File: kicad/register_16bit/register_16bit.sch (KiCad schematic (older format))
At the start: 0 parts

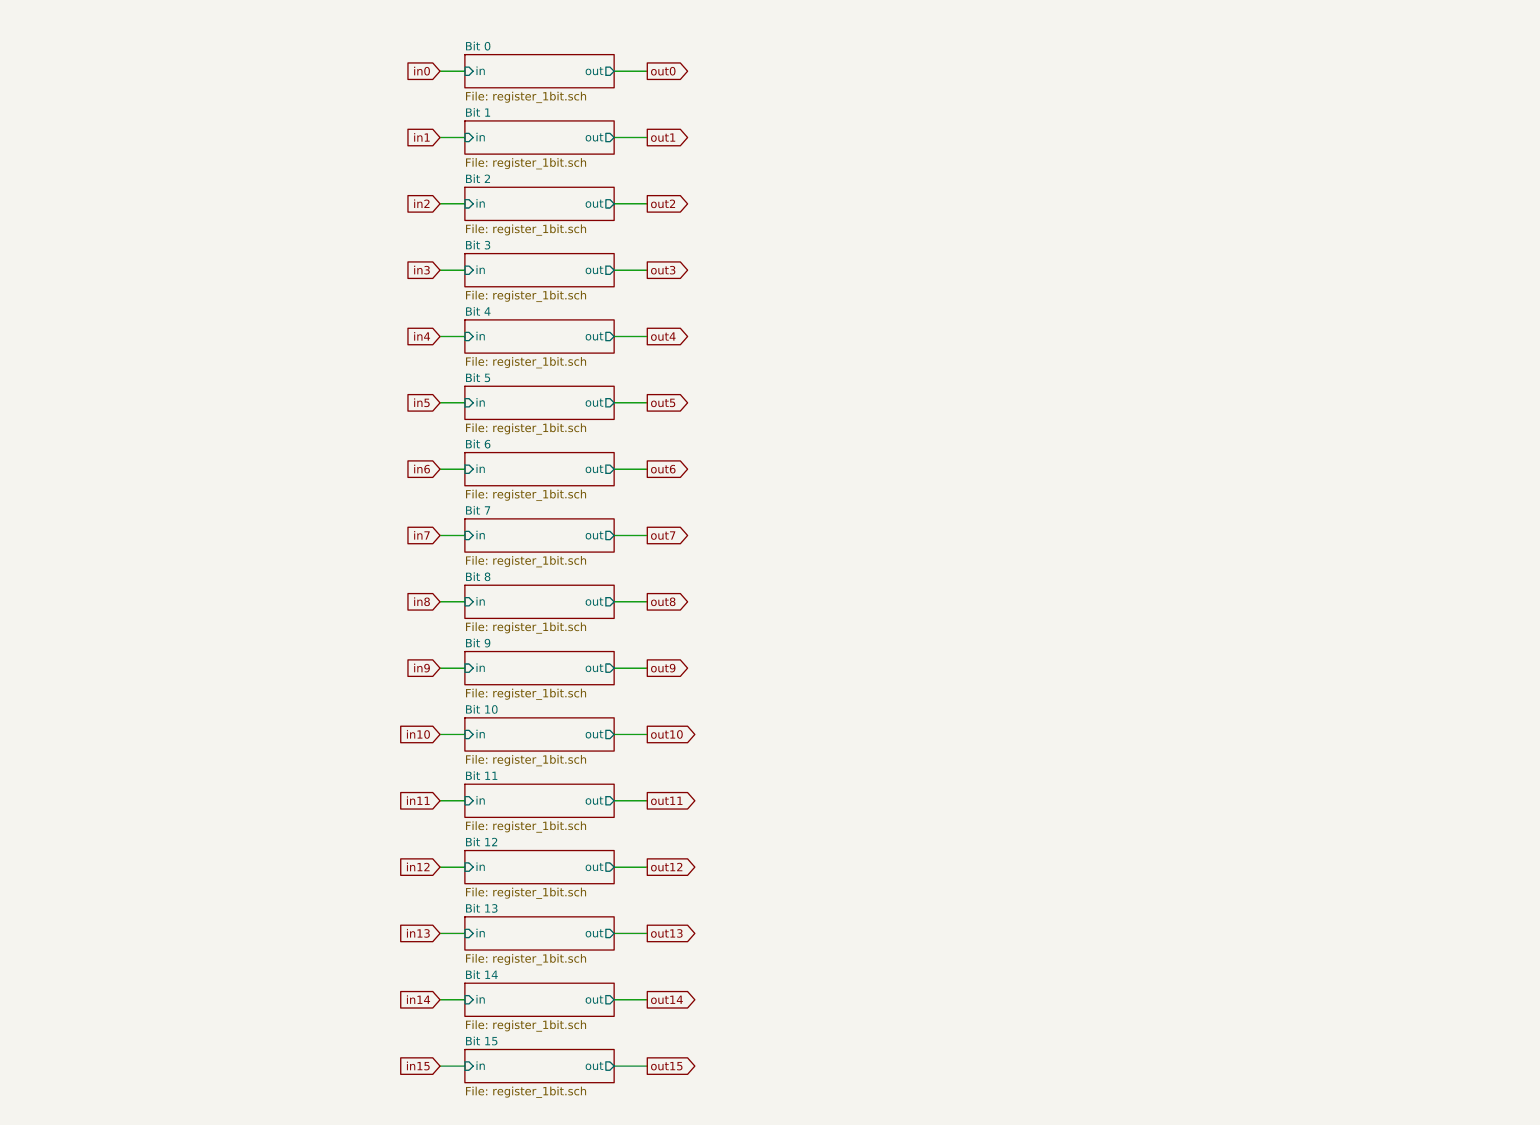
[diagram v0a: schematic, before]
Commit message: Finished initial PCB layout and routing for 16-bit register.
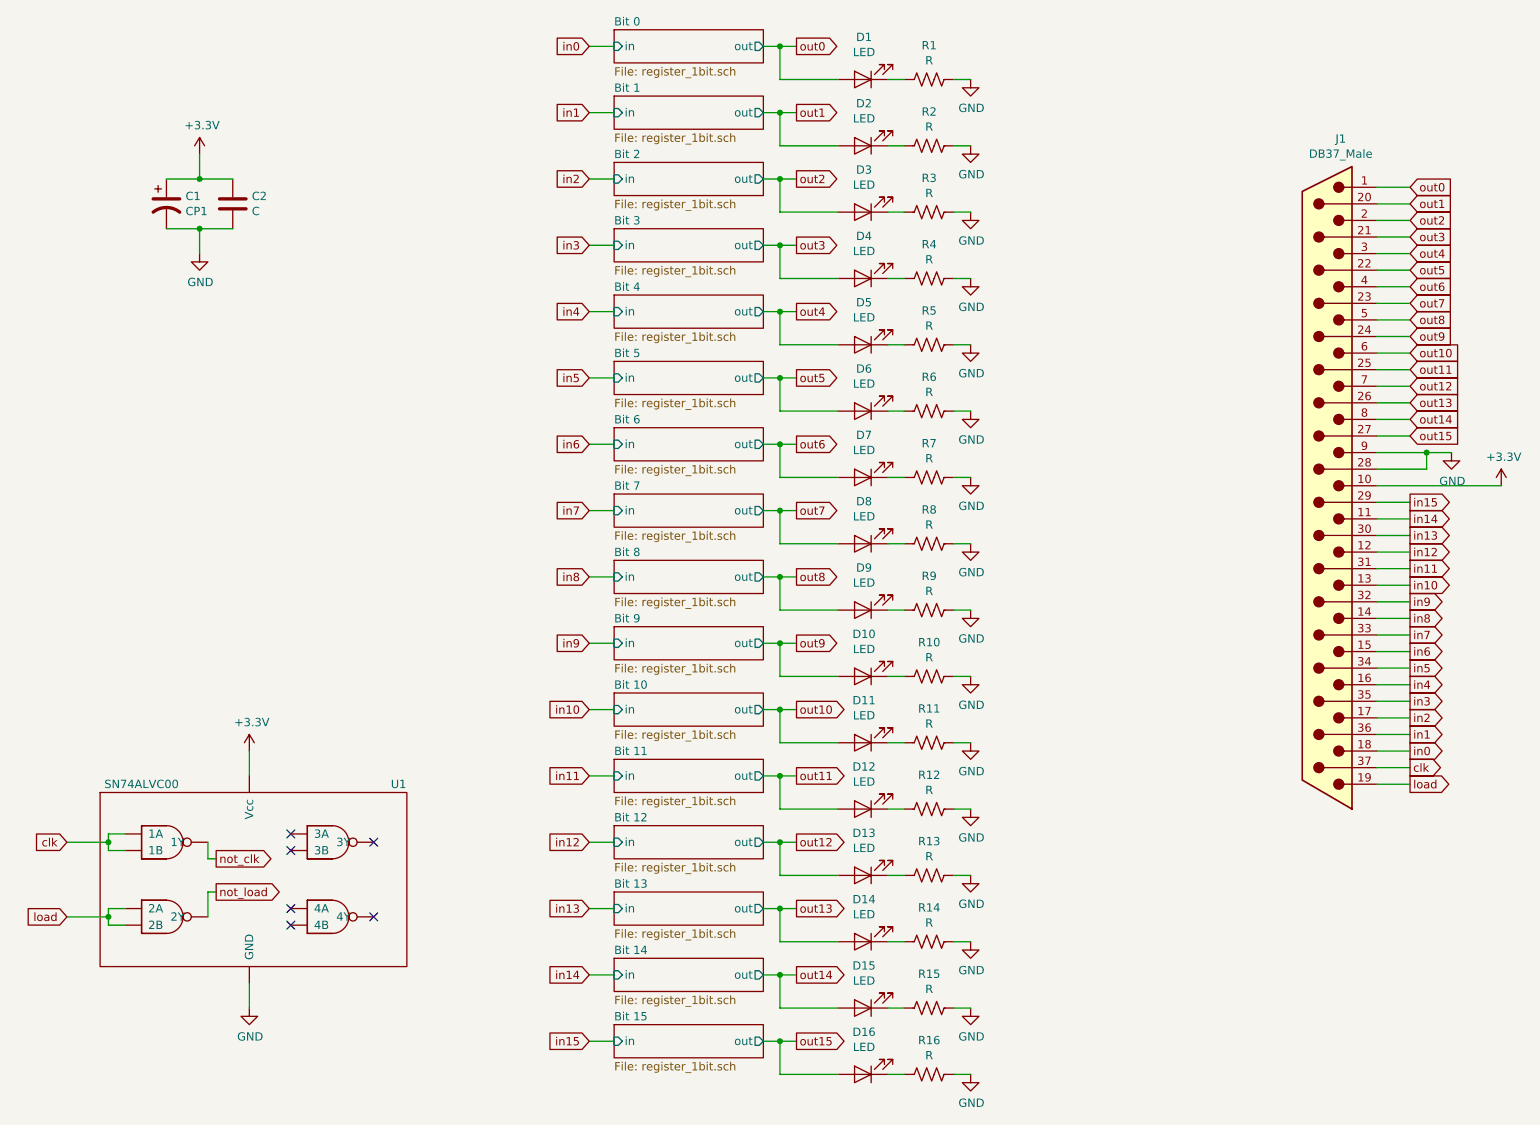
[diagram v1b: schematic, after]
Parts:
- added C1: CP1, Capacitor_THT:CP_Radial_D8.0mm_P2.50mm, symbol Device:CP1
- added C2: C, Capacitor_THT:C_Disc_D5.0mm_W2.5mm_P2.50mm, symbol Device:C
- added D1, D10, D11, D12, D13, D14, D15, D16, D2, D3, D4, D5, D6, D7, D8, D9: LED, LED_THT:LED_D5.0mm, symbol Device:LED
- added J1: DB37_Male, Connector_Dsub:DSUB-37_Male_Horizontal_P2.77x2.84mm_EdgePinOffset4.94mm_Housed_MountingHolesOffset7.48mm, symbol Connector:DB37_Male
- added R1, R10, R11, R12, R13, R14, R15, R16, R2, R3, R4, R5, R6, R7, R8, R9: R, Resistor_SMD:R_1206_3216Metric, symbol Device:R_US
- added U1: SN74ALVC00, Package_SO:TSSOP-14_4.4x5mm_P0.65mm, symbol NANDIRL_components:SN74ALVC00
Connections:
- net in0: now also J1.18
- net in1: now also J1.36
- net in10: now also J1.13
- net in11: now also J1.31
- net in12: now also J1.12
- net in13: now also J1.30
- net in14: now also J1.11
- net in15: now also J1.29
- net in2: now also J1.17
- net in3: now also J1.35
- net in4: now also J1.16
- net in5: now also J1.34
- net in6: now also J1.15
- net in7: now also J1.33
- net in8: now also J1.14
- net in9: now also J1.32
- net out0: now also D1.2 (A), J1.1
- net out1: now also D2.2 (A), J1.20
- net out10: now also D11.2 (A), J1.6
- net out11: now also D12.2 (A), J1.25
- net out12: now also D13.2 (A), J1.7
- net out13: now also D14.2 (A), J1.26
- net out14: now also D15.2 (A), J1.8
- net out15: now also D16.2 (A), J1.27
- net out2: now also D3.2 (A), J1.2
- net out3: now also D4.2 (A), J1.21
- net out4: now also D5.2 (A), J1.3
- net out5: now also D6.2 (A), J1.22
- net out6: now also D7.2 (A), J1.4
- net out7: now also D8.2 (A), J1.23
- net out8: now also D9.2 (A), J1.5
- net out9: now also D10.2 (A), J1.24
- new net: D1.1 (K), R1.2
- new net: D2.1 (K), R2.2
- new net: D3.1 (K), R3.2
- new net: D4.1 (K), R4.2
- new net: D5.1 (K), R5.2
- new net: D6.1 (K), R6.2
- new net: D7.1 (K), R7.2
- new net: D8.1 (K), R8.2
- new net: D9.1 (K), R9.2
- new net: D10.1 (K), R10.2
- new net: D11.1 (K), R11.2
- new net: D12.1 (K), R12.2
- new net: D13.1 (K), R13.2
- new net: D14.1 (K), R14.2
- new net: D15.1 (K), R15.2
- new net: D16.1 (K), R16.2
- new net +3V3: C1.1, C2.1, J1.10, U1.14 (Vcc)
- new net GND: C1.2, C2.2, J1.28, J1.9, R1.1, R10.1, R11.1, R12.1, R13.1, R14.1, R15.1, R16.1, R2.1, R3.1, R4.1, R5.1, R6.1, R7.1, R8.1, R9.1, U1.7 (GND)
- new net clk: J1.37, U1.1 (1A), U1.2 (1B)
- new net load: J1.19, U1.4 (2A), U1.5 (2B)
- new net not_clk: U1.3 (1Y)
- new net not_load: U1.6 (2Y)
- no-connect marks 0 -> 6

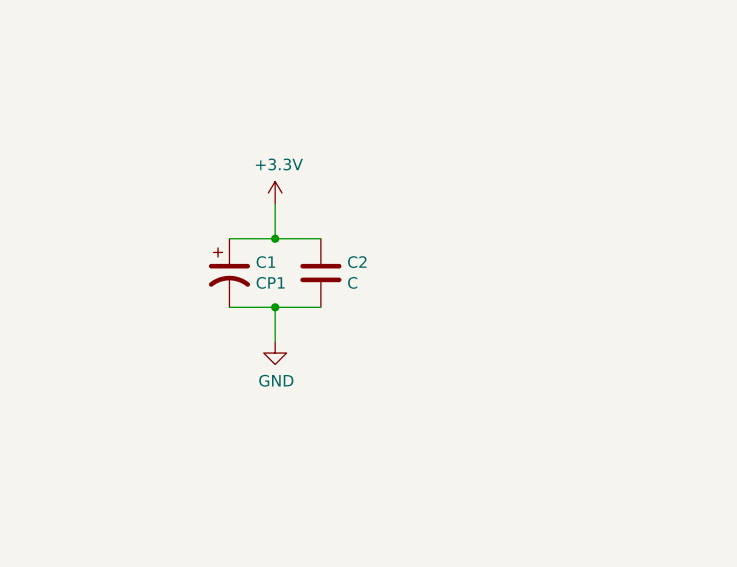
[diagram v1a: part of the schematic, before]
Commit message: Added clock generator, tested on breadboard. Added motherboard, routing unfinished. Various component updates.
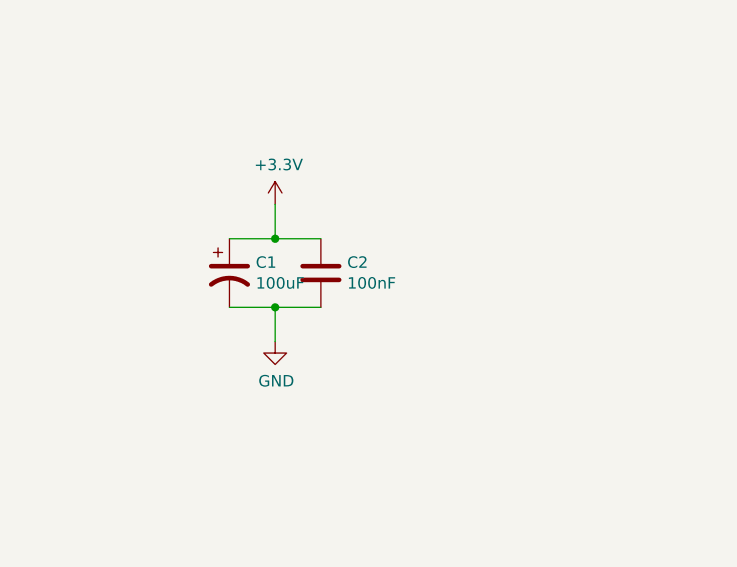
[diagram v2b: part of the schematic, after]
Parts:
- C1: value CP1 -> 100uF; Digikey PN (none) -> P15797CT-ND
- C2: value C -> 100nF; footprint Capacitor_THT:C_Disc_D5.0mm_W2.5mm_P2.50mm -> Capacitor_THT:C_Disc_D5.0mm_W2.5mm_P5.00mm; Digikey PN (none) -> BC5229CT-ND
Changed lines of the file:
@@
 P 1650 2000
 F 0 "C1" H 1765 2046 50  0000 L CNN
-F 1 "CP1" H 1765 1955 50  0000 L CNN
+F 1 "100uF" H 1765 1955 50  0000 L CNN
 F 2 "Capacitor_THT:CP_Radial_D8.0mm_P2.50mm" H 1650 2000 50  0001 C CNN
 F 3 "~" H 1650 2000 50  0001 C CNN
+F 4 "P15797CT-ND" H 1650 2000 50  0001 C CNN "Digikey PN"
 	1    1650 2000
 	1    0    0    -1
@@
 P 2050 2000
 F 0 "C2" H 2165 2046 50  0000 L CNN
-F 1 "C" H 2165 1955 50  0000 L CNN
-F 2 "Capacitor_THT:C_Disc_D5.0mm_W2.5mm_P2.50mm" H 2088 1850 50  0001 C CNN
+F 1 "100nF" H 2165 1955 50  0000 L CNN
+F 2 "Capacitor_THT:C_Disc_D5.0mm_W2.5mm_P5.00mm" H 2088 1850 50  0001 C CNN
 F 3 "~" H 2050 2000 50  0001 C CNN
+F 4 "BC5229CT-ND" H 2050 2000 50  0001 C CNN "Digikey PN"
 	1    2050 2000
 	1    0    0    -1

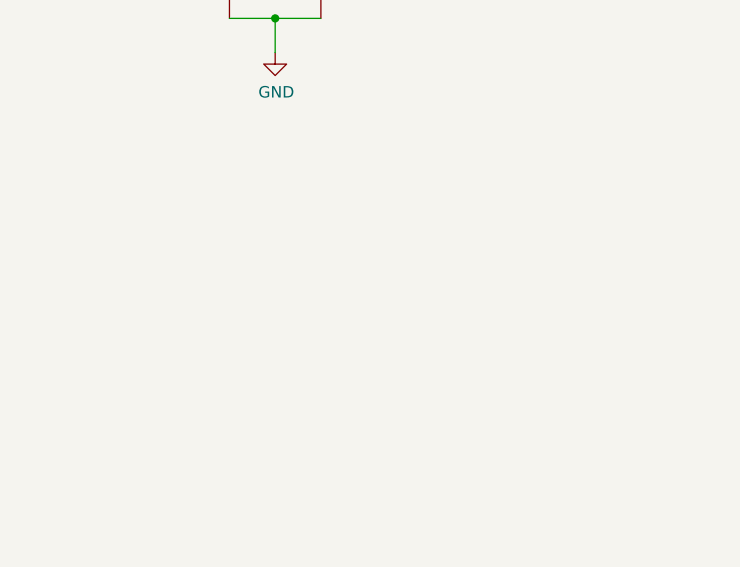
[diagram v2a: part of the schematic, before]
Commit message: ALU schematic, layout, routing complete. Associated motherboardmod. Also added Load LED to register and program counter boards.
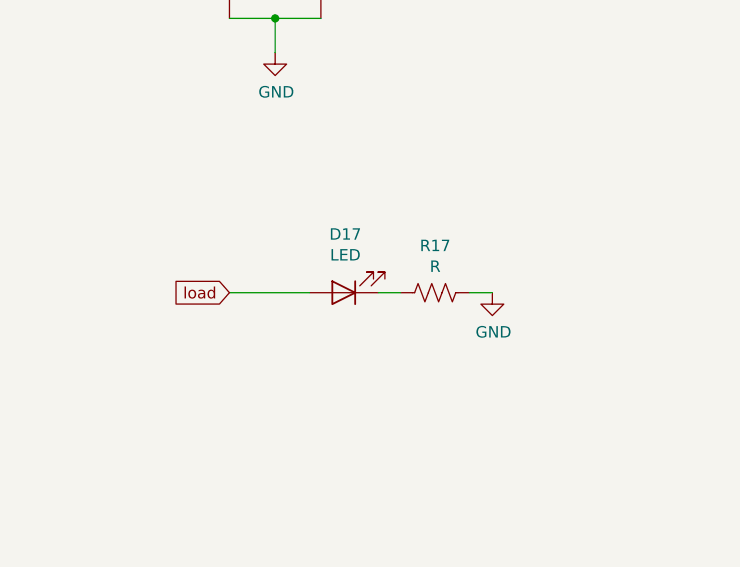
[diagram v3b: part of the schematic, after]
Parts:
- added D17: LED, LED_THT:LED_D5.0mm, symbol Device:LED
- added R17: R, Resistor_SMD:R_1206_3216Metric, symbol Device:R_US
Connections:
- net GND: now also R17.1
- net load: now also D17.2 (A)
- new net: D17.1 (K), R17.2
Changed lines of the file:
@@
 Wire Wire Line
 	8950 3700 9700 3700
+$Comp
+L Device:R_US R17
+U 1 1 5EA92581
+P 2550 3350
+F 0 "R17" V 2345 3350 50  0000 C CNN
+F 1 "R" V 2436 3350 50  0000 C CNN
+F 2 "Resistor_SMD:R_1206_3216Metric" V 2480 3350 50  0001 C CNN
+F 3 "~" H 2550 3350 50  0001 C CNN
+	1    2550 3350
+	0    1    1    0
+$EndComp
+Wire Wire Line
+	2300 3350 2400 3350
+$Comp
+L power:GND #PWR0219
+U 1 1 5EA92588
+P 2800 3350
+F 0 "#PWR0219" H 2800 3100 50  0001 C CNN
+F 1 "GND" H 2805 3177 50  0000 C CNN
+F 2 "" H 2800 3350 50  0001 C CNN
+F 3 "" H 2800 3350 50  0001 C CNN
+	1    2800 3350
+	1    0    0    -1
+$EndComp
+Wire Wire Line
+	2700 3350 2800 3350
+$Comp
+L Device:LED D17
+U 1 1 5EA9258F
+P 2150 3350
+F 0 "D17" H 2143 3095 50  0000 C CNN
+F 1 "LED" H 2143 3186 50  0000 C CNN
+F 2 "LED_THT:LED_D5.0mm" H 2150 3350 50  0001 C CNN
+F 3 "~" H 2150 3350 50  0001 C CNN
+	1    2150 3350
+	-1   0    0    1
+$EndComp
+Wire Wire Line
+	1650 3350 2000 3350
+Text GLabel 1650 3350 0    50   Input ~ 0
+load
 $EndSCHEMATC
